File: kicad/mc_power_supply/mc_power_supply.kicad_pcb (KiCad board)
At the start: 2 copper layers, 118 x 65 mm, 4 parts

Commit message: Приступил к расположению компонентов на плате mc_power_supply_ver3.
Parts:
- added C1: 1 мк 275В, IWcomponents:CAPACITOR_B32923_26.5x11, F.Cu at (124.5, 85.3)
- added C2: 1 мк 275В, IWcomponents:CAPACITOR_B32923_26.5x11, F.Cu at (161.0, 92.5)
- added C3: 4700 мк 35 В, IWcomponents:CAPACITOR_10_D22, F.Cu at (159.5, 119.4)
- added C4: 470 мк 35 В, IWcomponents:CAPACITOR_5.08_D10, F.Cu at (224.0, 130.6)
- added C5: 0.1 мк, IWsmd_case:SMD0805, F.Cu at (218.4, 84.8)
- added DA1: LM317D2T-TR, Package_TO:TO-263-3_TabPin2, F.Cu at (187.3, 118.9)
- added FU1: 0.25 A, IWcomponents:FU_PTF15B, F.Cu at (118.9, 73.7)
- added LL1: B82731T2301A020, IWtransformator:EMI_EPCOS_B82731T, F.Cu at (161.0, 75.2)
- added R1: 500 к, IWsmd_case:SMD2512, F.Cu at (140.7, 79.8)
- added R2: 240, IWsmd_case:SMD0805, F.Cu at (226.1, 83.8)
- added R3: 5 к, IWsmd_case:BOURNS_3224W, F.Cu at (226.3, 96.5)
- added RU1: B72210S0271K101, IWcomponents:RU_EPCOS_B72210S0271K101_12х5, F.Cu at (146.3, 79.2)
- added TV1: ТПГ-112-12, IWtransformator:TPG112-12, F.Cu at (123.4, 111.8)
- added VD1: VS-10MQ100NTRPBF, IWcomponents:SMA, F.Cu at (214.2, 105.8)
- added VD2: VS-10MQ100NTRPBF, IWcomponents:SMA, F.Cu at (218.3, 96.4)
- added VD3: VS-10MQ100NTRPBF, IWcomponents:SMA, F.Cu at (220.1, 90.1)
- added VD4: VS-10MQ100NTRPBF, IWcomponents:SMA, F.Cu at (218.3, 101.0)
- added VD5: VS-10MQ100NTRPBF, IWcomponents:SMA, F.Cu at (223.9, 105.8)
- added XP1: L-KLS8-01128-PC-250-0.8, IWconnectors:TERMINAL_KLS8-01128_6.3mm, F.Cu at (103.6, 78.2)
- added XP2: L-KLS8-01128-PC-250-0.8, IWconnectors:TERMINAL_KLS8-01128_6.3mm, F.Cu at (103.6, 85.3)
- added XP3: WF-2, IWconnectors:WF-2, F.Cu at (228.4, 91.5)

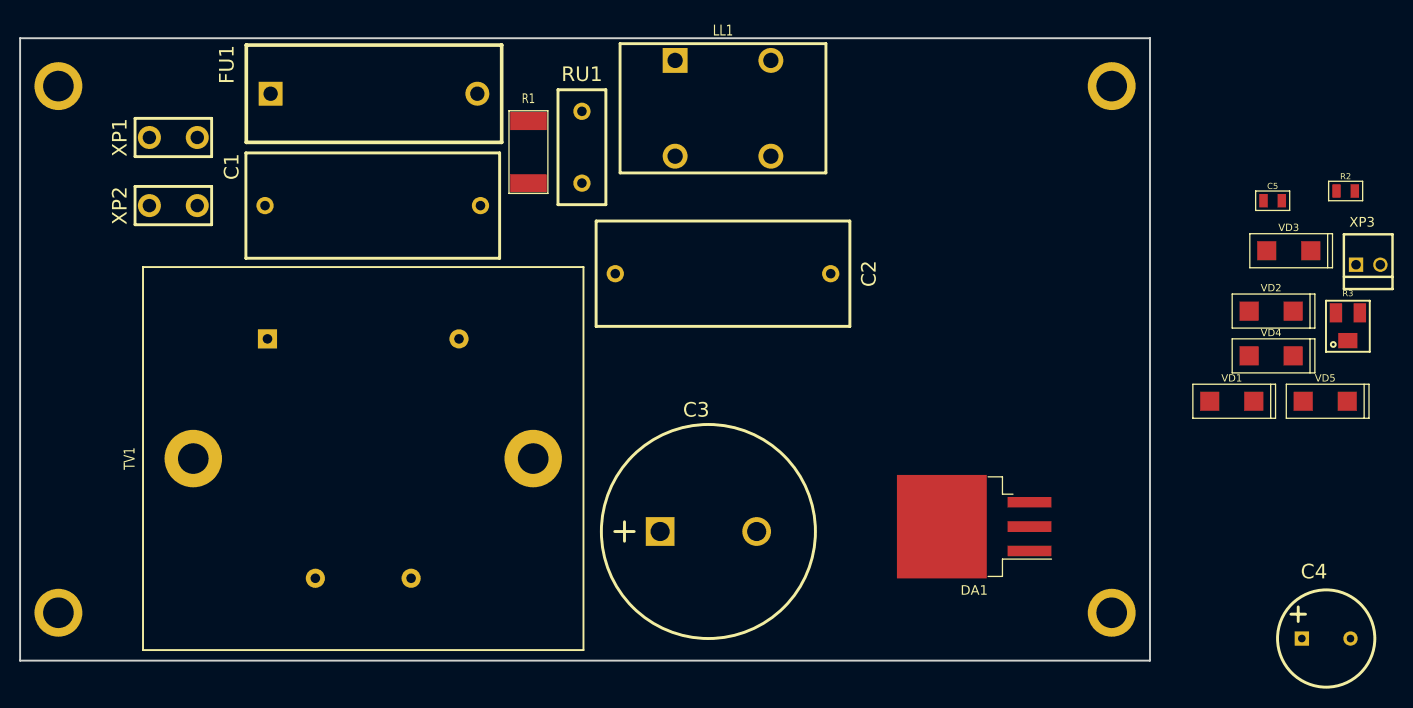
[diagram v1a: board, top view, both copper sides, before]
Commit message: Закончил предварительную трассировку плат MM power supply ver. 3.0.
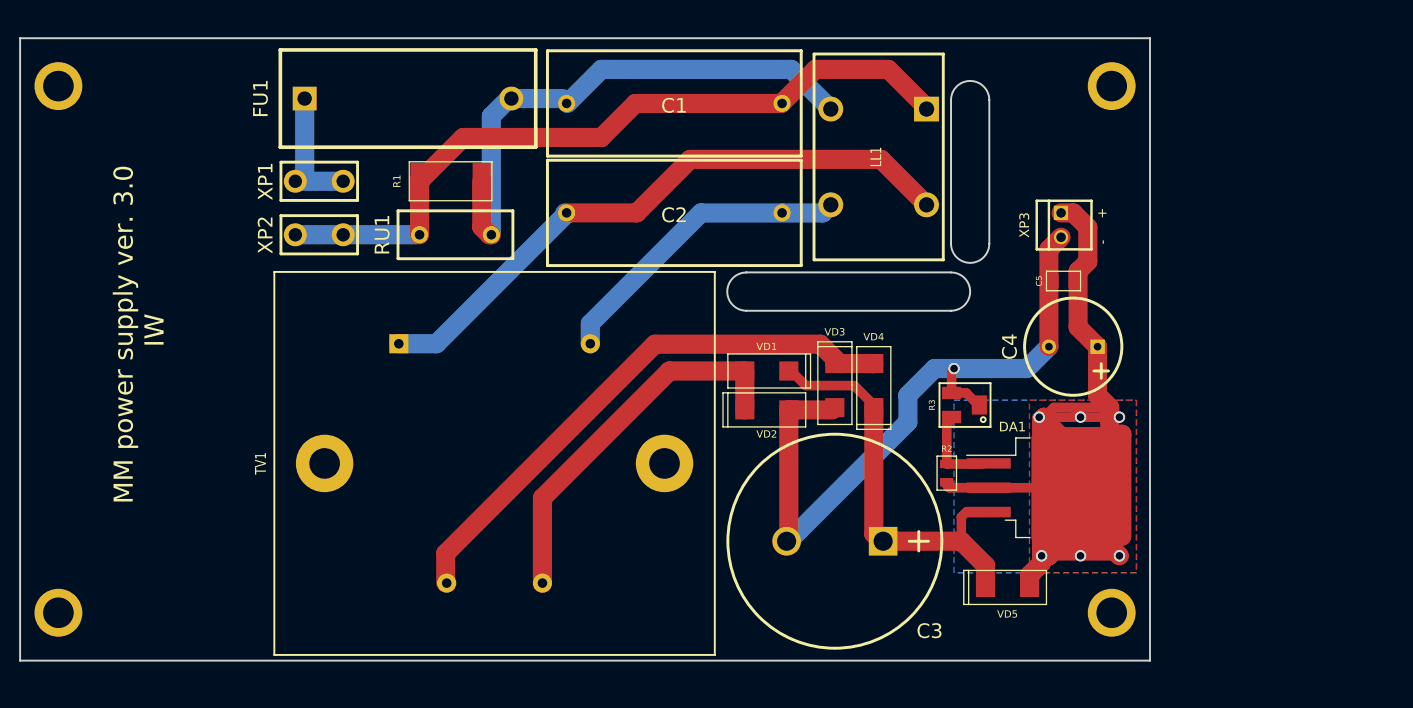
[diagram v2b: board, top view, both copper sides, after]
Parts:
- moved VD2 53.7 mm to (165.6, 106.7), turned to 180 degrees
- moved R2 51.0 mm to (184.4, 113.3), turned to 270 degrees
- moved VD3 49.4 mm to (172.7, 104.1), turned to 90 degrees
- moved VD1 48.7 mm to (165.6, 102.6)
- moved R3 42.5 mm to (184.9, 106.2), turned to 90 degrees
- moved VD4 41.6 mm to (176.8, 104.1), turned to 270 degrees
- moved C4 40.3 mm to (197.6, 100.1), turned to 180 degrees
- moved VD5 38.5 mm to (190.8, 125.2), turned to 180 degrees
- moved C1 33.3 mm to (156.0, 74.7), turned to 0 degrees
- moved XP3 32.3 mm to (196.3, 87.4), turned to 270 degrees
- moved C5 23.4 mm to (196.6, 93.2), turned to 180 degrees
- moved LL1 17.0 mm to (177.3, 80.3), turned to 270 degrees
- moved RU1 16.1 mm to (133.1, 88.4), turned to 180 degrees
- moved XP1 15.9 mm to (118.9, 82.8)
- moved XP2 15.5 mm to (118.9, 88.4)
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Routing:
- net Net-(C4-Pad1): track 0.00 -> 123.8 mm, vias 0 -> 6
- net Net-(C1-Pad2): track 0.00 -> 78.4 mm
- net /GND: track 0.00 -> 73.9 mm, vias 0 -> 1
- net Net-(C2-Pad2): track 0.00 -> 64.9 mm
- net Net-(TV1-Pad9): track 0.00 -> 58.0 mm
- net Net-(C1-Pad1): track 0.00 -> 57.1 mm
- net Net-(C3-Pad1): track 0.00 -> 44.7 mm
- net Net-(TV1-Pad7): track 0.00 -> 39.6 mm
- net Net-(C2-Pad1): track 0.00 -> 32.1 mm
- net Net-(FU1-Pad1): track 0.00 -> 14.1 mm
- net Net-(DA1-Pad1): track 0.00 -> 8.95 mm
- added copper zone on B.Cu, net Net-(C4-Pad1)
- added copper zone on F.Cu, net Net-(C4-Pad1)
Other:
- outline, holes or cut-outs redrawn
- board text added: "+"
- board text added: "-"
- board text added: "MM power supply ver. 3.0 IW"

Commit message: Заменил трансформатор на плате MM power supply ver. 3.0. и приступил к повторной трассировке.
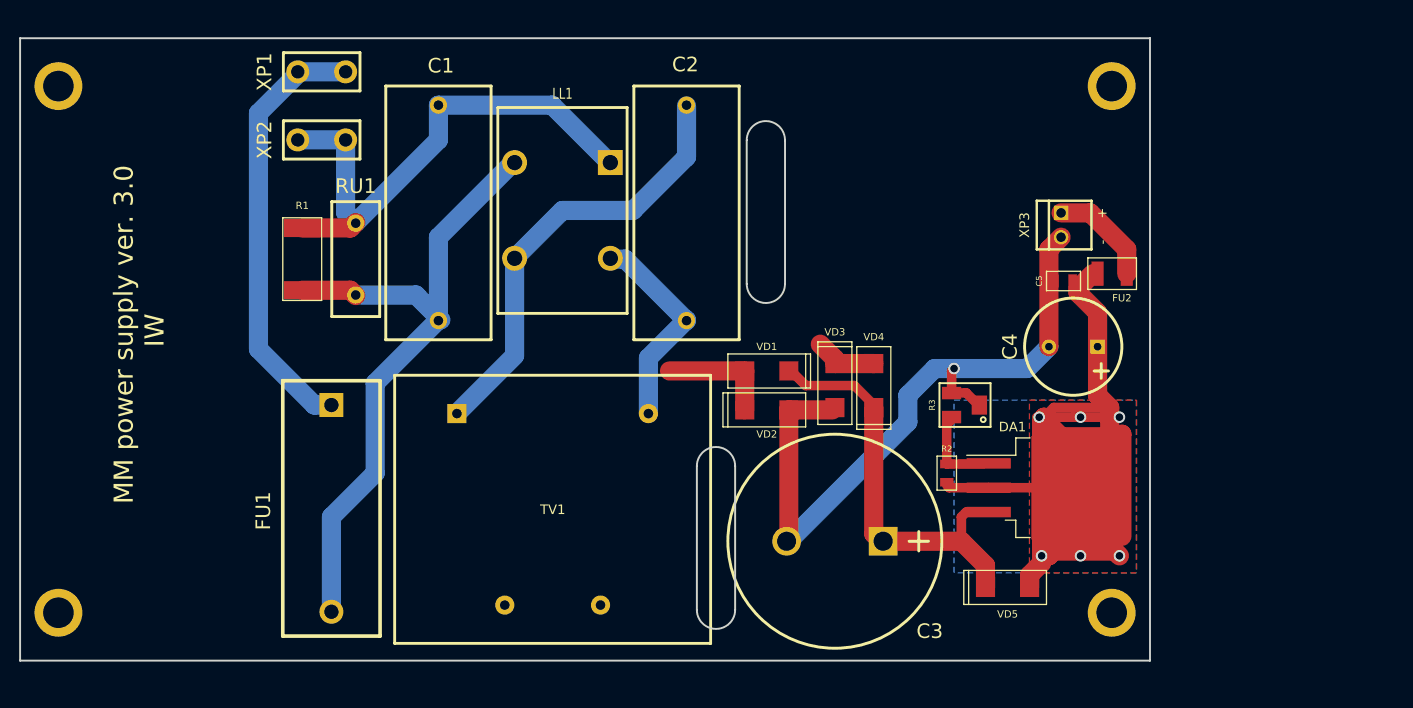
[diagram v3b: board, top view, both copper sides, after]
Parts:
- added FU2: MF-USMF020-2, IWsmd_case:SMD1210, F.Cu at (201.7, 92.5)
- C1, C2: value 1 мк 275В -> 1 мк 305В
- FU1: value 0.25 A -> 0.1 A
- TV1: value ТПГ-112-12 -> ТПГ-2-12; footprint IWtransformator:TPG112-12 -> IWtransformator:TPG2-12
- moved FU1 37.2 mm to (120.1, 111.3), turned to 270 degrees
- moved LL1 33.5 mm to (144.3, 85.9)
- moved C1 27.2 mm to (131.3, 86.1), turned to 90 degrees
- moved R1 17.5 mm to (117.1, 90.9), turned to 270 degrees
- moved XP1 11.4 mm to (119.1, 71.4)
- moved RU1 10.7 mm to (122.7, 90.9), turned to 90 degrees
- moved XP2 9.91 mm to (119.1, 78.5)
- moved TV1 7.78 mm to (143.3, 117.1)
- moved C2 1.27 mm to (157.2, 86.1), turned to 90 degrees
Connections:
- LL1 pad 3: Net-(C2-Pad1) -> Net-(C2-Pad2)
- LL1 pad 4: Net-(C2-Pad2) -> Net-(C2-Pad1)
- XP3 pad 1: Net-(C4-Pad1) -> Net-(FU2-Pad2)
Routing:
- net Net-(TV1-Pad9): track 58.0 -> 6.74 mm
- net Net-(FU1-Pad1): track 14.1 -> 45.6 mm
- net Net-(TV1-Pad7): track 39.6 -> 11.9 mm
- net Net-(C1-Pad2): track 78.4 -> 56.0 mm
- net Net-(C2-Pad2): track 64.9 -> 46.2 mm
- net Net-(C1-Pad1): track 57.1 -> 70.7 mm
- net Net-(FU2-Pad2): track 0.00 -> 11.0 mm
- net Net-(C2-Pad1): track 32.1 -> 22.0 mm
- net Net-(C4-Pad1): track 123.8 -> 115.7 mm
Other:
- outline, holes or cut-outs redrawn

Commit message: Повторно произвёл трассировку платы mc_power_supply_ver_3.0.
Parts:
- moved C3 30.7 mm to (180.6, 90.7), turned to 0 degrees
- moved VD1 22.9 mm to (171.4, 124.7), turned to 90 degrees
- moved VD2 20.6 mm to (175.5, 124.7), turned to 270 degrees
- moved VD3 13.5 mm to (173.0, 117.6), turned to 180 degrees
- moved XP3 10.2 mm to (193.8, 77.5), turned to 180 degrees
- moved VD4 10.1 mm to (173.0, 113.5), turned to 0 degrees
- moved FU2 4.68 mm to (198.6, 88.9), turned to 90 degrees
- moved LL1 0.25 mm to (144.3, 86.1)
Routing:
- net Net-(C3-Pad1): track 44.7 -> 83.0 mm, vias 0 -> 1
- net Net-(TV1-Pad9): track 6.74 -> 40.6 mm
- net Net-(C2-Pad2): track 46.2 -> 73.9 mm
- net /GND: track 73.9 -> 89.1 mm
- net Net-(TV1-Pad7): track 11.9 -> 27.0 mm
- net Net-(C4-Pad1): track 115.7 -> 117.6 mm
- net Net-(C1-Pad1): track 70.7 -> 71.6 mm
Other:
- outline, holes or cut-outs redrawn

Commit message: Поправил трассировку на платы mc_power_supply_ver_3.0.
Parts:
- DA1: footprint Package_TO:TO-263-3_TabPin2 -> IWsmd_case:TO-252-3_TabPin_2
- R1: value 500 к -> 510 к
- moved DA1 0.76 mm to (193.8, 114.8)
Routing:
- net Net-(C4-Pad1): track 117.6 -> 102.8 mm, vias 6 -> 8

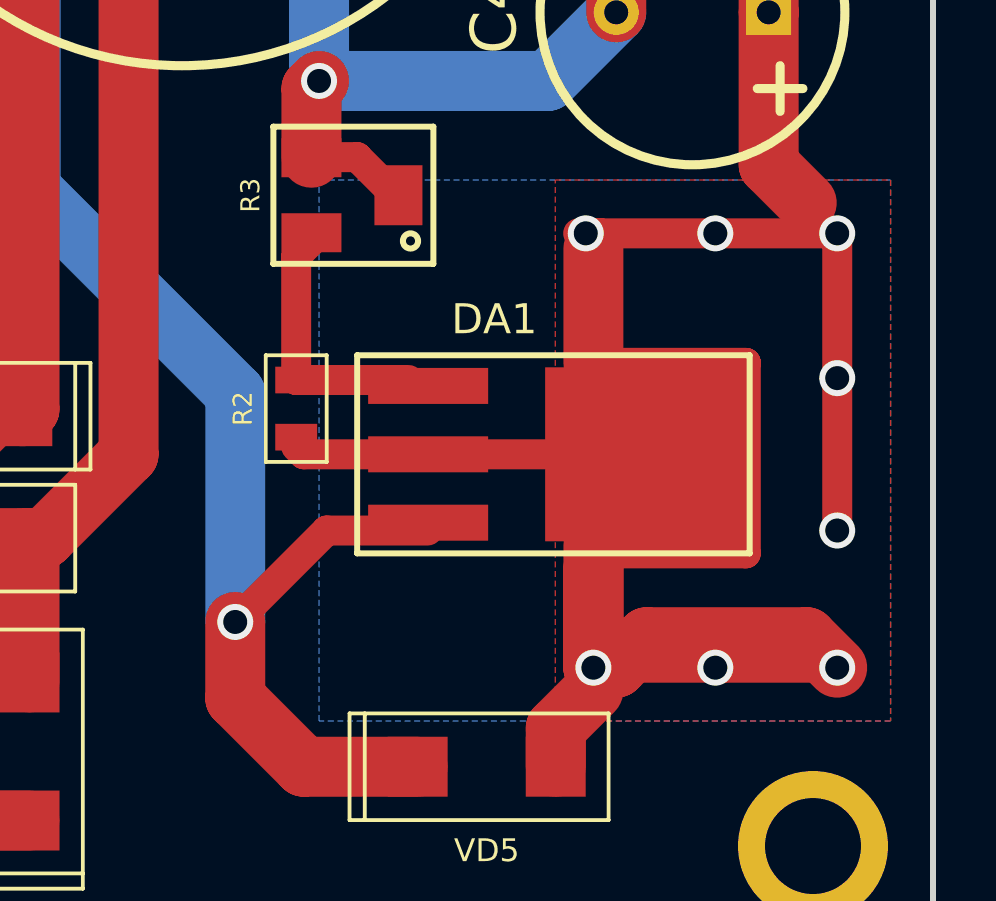
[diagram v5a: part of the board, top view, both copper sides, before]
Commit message: Поравил плату mc_power_supply ver.3.
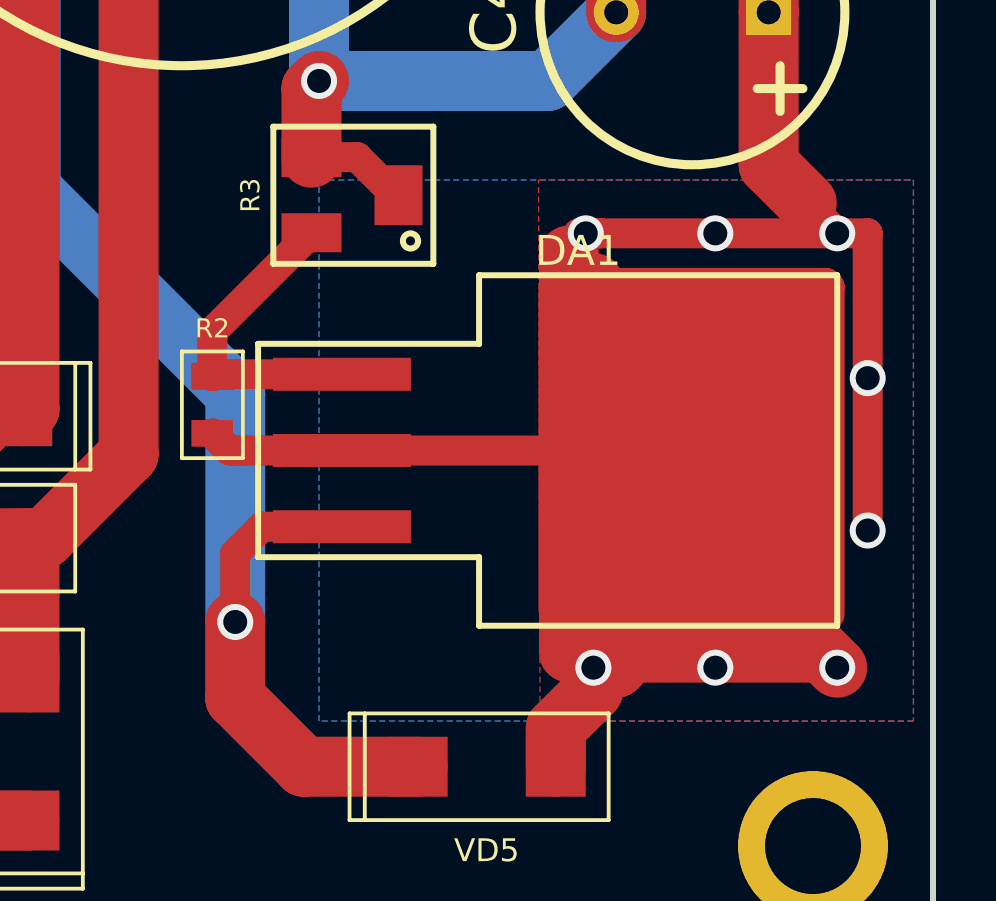
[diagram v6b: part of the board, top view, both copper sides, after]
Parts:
- DA1: footprint IWsmd_case:TO-252-3_TabPin_2 -> IWsmd_case:TO-263-3_TabPin_2
- moved R2 2.80 mm to (181.6, 113.2)
- moved DA1 0.13 mm to (193.8, 114.7)
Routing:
- net Net-(C4-Pad1): track 102.8 -> 150.1 mm
- net Net-(DA1-Pad1): track 8.95 -> 10.5 mm
- net Net-(C3-Pad1): track 83.0 -> 81.5 mm

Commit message: Продолжил разрабатывать плату mc_power_supply.
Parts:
- turned LL1 to 90 degrees
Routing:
- net Net-(C2-Pad2): track 73.9 -> 55.1 mm
- net Net-(C1-Pad2): track 56.0 -> 49.5 mm
- net Net-(C1-Pad1): track 71.6 -> 70.6 mm

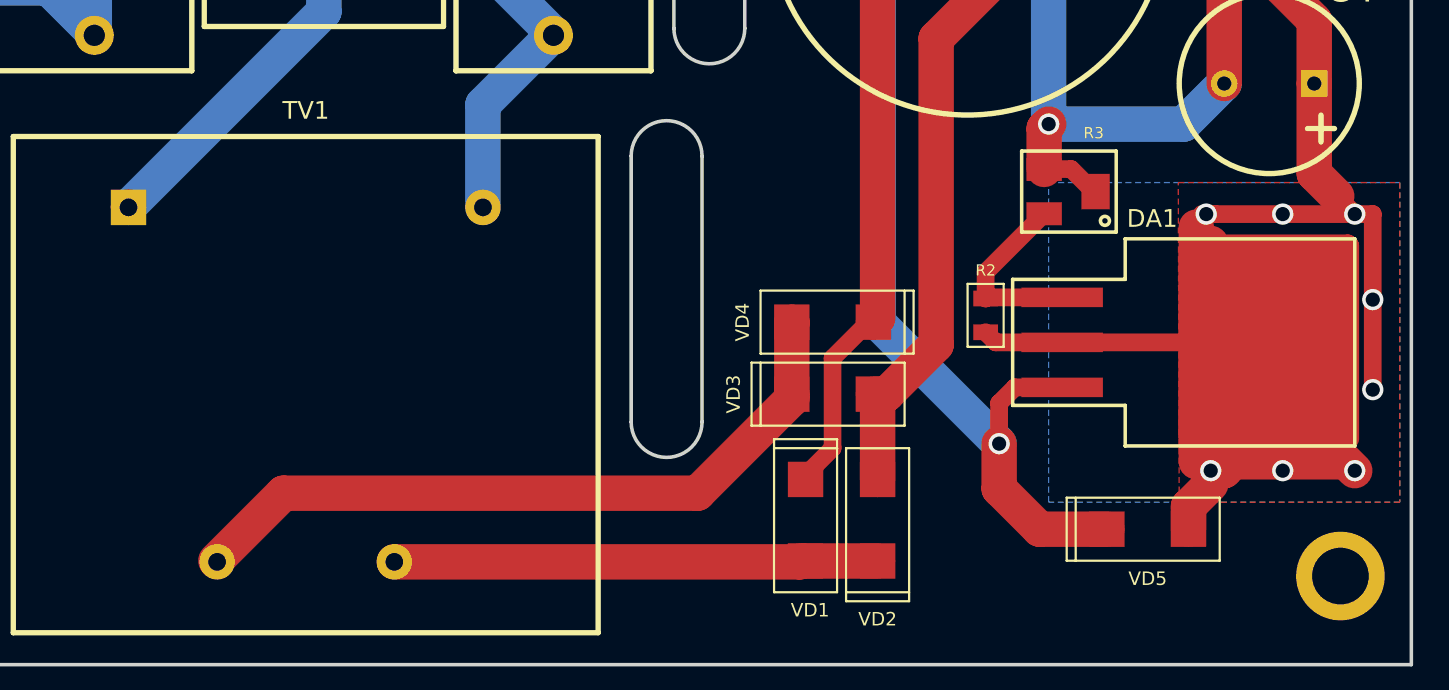
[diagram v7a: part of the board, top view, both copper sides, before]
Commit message: Отправил печатную плату mc_power_supply в производство.
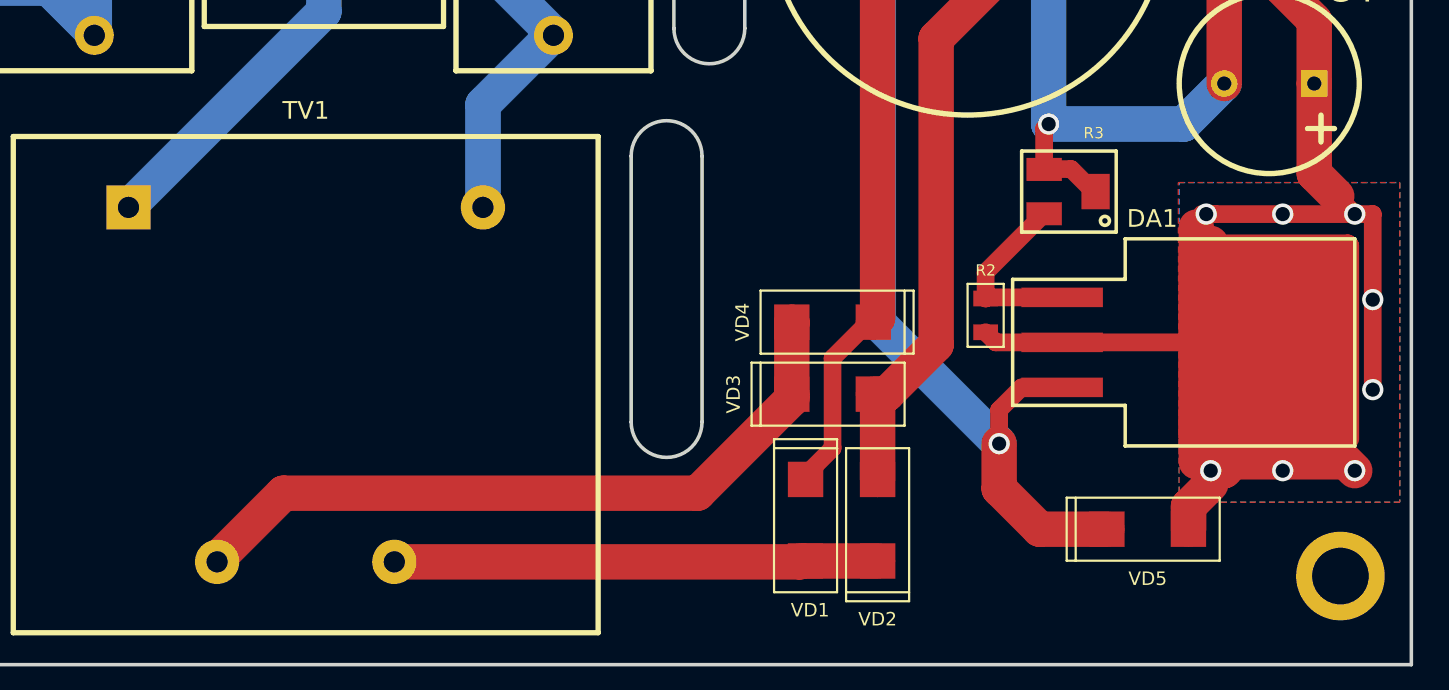
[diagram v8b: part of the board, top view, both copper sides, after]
